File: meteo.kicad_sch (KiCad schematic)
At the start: 26 parts, among them J1 mlab I2C, J10 Eth, J11 I2C0, J12 I2C1, J13 I2C2, J14 I2C3, J15 UART, J16 UART pow, J17 5V jumper, J18 power control circuit, J2 SPI, J3 Analog, J4 Conn_02x19_Odd_Even, J5 Conn_02x18_Odd_Even, J6 I/O, J9 SD, U1 CD74HC4067M, U2 CD74HC4067M, U3 multiplex analog, U4 ADS1015IDGS, U5 PCF8575DBR

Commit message: Uploading newer version
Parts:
- added R3, R4: R, Resistor_THT:R_Axial_DIN0207_L6.3mm_D2.5mm_P15.24mm_Horizontal, symbol Device:R
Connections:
- net 5V: now also J18.3 (Pin_3), R3.2, R4.2; no longer J18.1 (Pin_1)
- net GND: now also U1.15 (~{E}), U2.15 (~{E}), U3.15 (~{E})
- net HW_reset: now also J18.1 (Pin_1); no longer J18.3 (Pin_3)
- net SCL: now also R4.1
- net SDA: now also R3.1
- no-connect marks 16 -> 13
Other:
- moved on the sheet: D1, D2, R1, R2

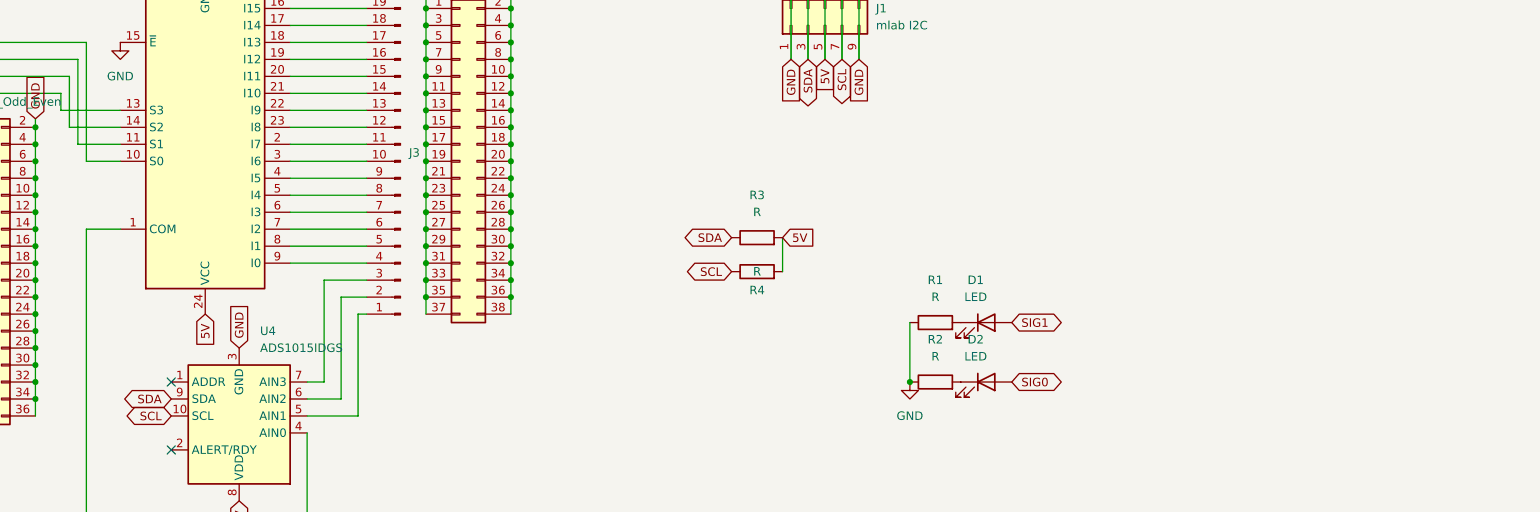
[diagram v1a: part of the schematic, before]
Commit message: Adding pins for power and pullup ressistors for I2C
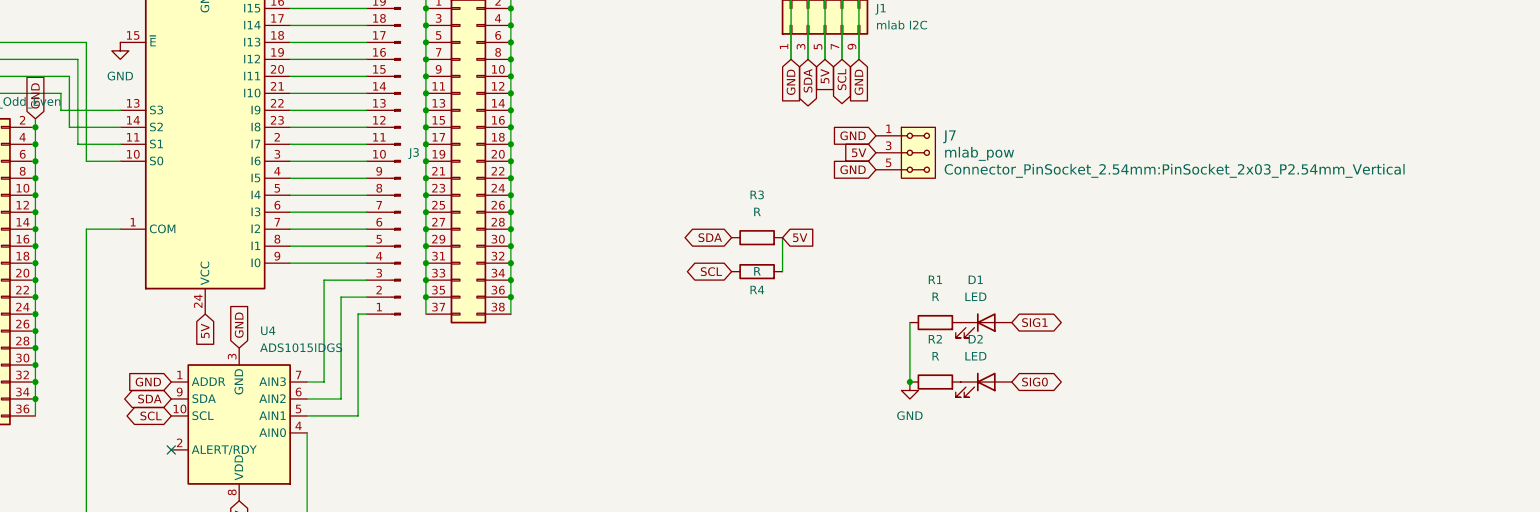
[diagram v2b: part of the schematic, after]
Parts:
- added J7: mlab_pow, Connector_PinSocket_2.54mm:PinSocket_2x03_P2.54mm_Vertical, symbol MLAB_HEADER:HEADER_2x03_PARALLEL
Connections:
- net 5V: now also J7.3, J7.4
- net GND: now also U4.1 (ADDR), J7.1, J7.2, J7.5, J7.6
- no-connect marks 13 -> 12
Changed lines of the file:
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@@
 	)
 	(no_connect
-		(at 147.32 161.29)
-	)
-	(no_connect
 		(at 73.66 134.62)
 	)
@@
 		)
 	)
+	(global_label "5V"
+		(shape input)
+		(at 252.73 127 180)
+		(effects
+			(font
+				(size 1.27 1.27)
+			)
+			(justify right)
+		)
+		(property "Intersheetrefs" "${INTERSHEET_REFS}"
+			(at 252.73 127 90)
+			(hide yes)
+			(show_name no)
+			(do_not_autoplace no)
+			(effects
+				(font
+					(size 1.27 1.27)
+				)
+			)
+		)
+	)
 	(global_label "GND"
 		(shape input)
@@
 		)
 	)
+	(global_label "GND"
+		(shape input)
+		(at 252.73 124.46 180)
+		(effects
+			(font
+				(size 1.27 1.27)
+			)
+			(justify right)
+		)
+		(property "Intersheetrefs" "${INTERSHEET_REFS}"
+			(at 252.73 124.46 90)
+			(hide yes)
+			(show_name no)
+			(do_not_autoplace no)
+			(effects
+				(font
+					(size 1.27 1.27)
+				)
+			)
+		)
+	)
 	(global_label "TX0"
 		(shape bidirectional)
@@
 		)
 	)
+	(global_label "GND"
+		(shape input)
+		(at 147.32 161.29 180)
+		(effects
+			(font
+				(size 1.27 1.27)
+			)
+			(justify right)
+		)
+		(property "Intersheetrefs" "${INTERSHEET_REFS}"
+			(at 147.32 161.29 90)
+			(hide yes)
+			(show_name no)
+			(do_not_autoplace no)
+			(effects
+				(font
+					(size 1.27 1.27)
+				)
+			)
+		)
+	)
 	(global_label "5V"
 		(shape input)
@@
 		)
 	)
+	(global_label "GND"
+		(shape input)
+		(at 252.73 129.54 180)
+		(effects
+			(font
+				(size 1.27 1.27)
+			)
+			(justify right)
+		)
+		(property "Intersheetrefs" "${INTERSHEET_REFS}"
+			(at 252.73 129.54 90)
+			(hide yes)
+			(show_name no)
+			(do_not_autoplace no)
+			(effects
+				(font
+					(size 1.27 1.27)
+				)
+			)
+		)
+	)
 	(global_label "CS1"
 		(shape bidirectional)
@@
 					(unit 1)
 				)
+			)
+		)
+	)
+	(symbol
+		(lib_id "MLAB_HEADER:HEADER_2x03_PARALLEL")
+		(at 259.08 127 0)
+		(unit 1)
+		(body_style 1)
+		(exclude_from_sim no)
+		(in_bom yes)
+		(on_board yes)
+		(in_pos_files yes)
+		(dnp no)
+		(fields_autoplaced yes)
+		(property "Reference" "J7"
+			(at 262.89 124.4599 0)
+			(show_name no)
+			(do_not_autoplace no)
+			(effects
+				(font
+					(size 1.524 1.524)
+				)
+				(justify left)
+			)
+		)
+		(property "Value" "mlab_pow"
+			(at 262.89 126.9999 0)
+			(show_name no)
+			(do_not_autoplace no)
+			(effects
+				(font
+					(size 1.524 1.524)
+				)
+				(justify left)
+			)
+		)
+		(property "Footprint" "Connector_PinSocket_2.54mm:PinSocket_2x03_P2.54mm_Vertical"
+			(at 262.89 129.5399 0)
+			(show_name no)
+			(do_not_autoplace no)
+			(effects
+				(font
+					(size 1.524 1.524)
+				)
+				(justify left)
+			)
+		)
+		(property "Datasheet" ""
+			(at 259.08 124.46 0)
+			(show_name no)
+			(do_not_autoplace no)
+			(effects
+				(font
+					(size 1.524 1.524)
+				)
+			)
+		)
+		(property "Description" "2x03 2.54 mm pitch header, 2 pins next to each other are connected"
+			(at 259.08 127 0)
+			(hide yes)
+			(show_name no)
+			(do_not_autoplace no)
+			(effects
+				(font
+					(size 1.27 1.27)
+				)
+			)
+		)
+		(pin "5"
+		)
+		(pin "3"
+		)
+		(pin "4"
+		)
+		(pin "6"
+		)
+		(pin "1"
+		)
+		(pin "2"
+		)
+		(instances
+			(project "meteo"
+				(path "/62b52698-682b-43ba-8570-59cdc1d6eb35"
+					(reference "J7")
+					(unit 1)
+				)

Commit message: Oprava děr
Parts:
- added H1, H2, H3, H4: MountingHole_Pad, MountingHole:MountingHole_3.2mm_M3_DIN965_Pad, symbol Mechanical:MountingHole_Pad
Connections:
- net GND: now also H1.1, H2.1, H3.1, H4.1
